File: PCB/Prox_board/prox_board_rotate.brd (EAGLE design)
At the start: 12 x 11 mm, 7 parts, among them U1 MAX44000

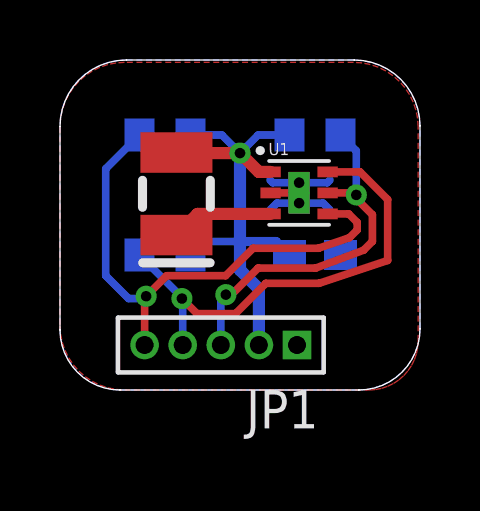
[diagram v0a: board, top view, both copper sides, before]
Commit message: Fix naming and silkscreen on the back of the board!
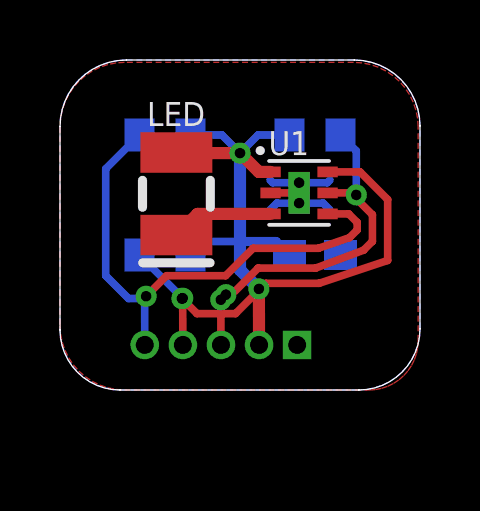
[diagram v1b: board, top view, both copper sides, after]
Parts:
- flipped JP1 to the bottom, turned to 0 degrees
- renumbered U$2 to LED
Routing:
- net SDA: track 15.8 -> 15.7 mm, vias 1 -> 2
- net VDD: vias 1 -> 2
- net SCL: vias 2 -> 3
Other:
- board text added: "LED"
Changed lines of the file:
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@@
 <layer number="23" name="tOrigins" color="15" fill="1" visible="yes" active="yes"/>
 <layer number="24" name="bOrigins" color="15" fill="1" visible="yes" active="yes"/>
-<layer number="25" name="tNames" color="7" fill="1" visible="no" active="yes"/>
-<layer number="26" name="bNames" color="7" fill="1" visible="no" active="yes"/>
+<layer number="25" name="tNames" color="7" fill="1" visible="yes" active="yes"/>
+<layer number="26" name="bNames" color="7" fill="1" visible="yes" active="yes"/>
 <layer number="27" name="tValues" color="7" fill="1" visible="no" active="yes"/>
 <layer number="28" name="bValues" color="7" fill="1" visible="no" active="yes"/>
@@
 <wire x1="12" y1="2.0366625" x2="12" y2="8.805565625" width="0" layer="20"/>
 <wire x1="12" y1="8.805565625" x2="9.805565625" y2="11" width="0" layer="20" curve="90"/>
+<text x="2.9" y="8.8" size="0.8" layer="25" ratio="14">LED</text>
 </plain>
 <attributes>
@@
 </autorouter>
 <elements>
-<element name="C1" library="resistor" package="C0603" value="0.1uF" x="8.5" y="4.5" rot="MR180"/>
-<element name="JP1" library="Wisp5_Harvester_Motor-driver_V2" package="PINHEAD_1X05-1.27MM" value="PINHEAD_PINHD-1X5-1.27MM" x="5.36" y="1.5" rot="R180"/>
-<element name="R1" library="resistor" package="R0603" value="DNP" x="3.5" y="8.5" rot="MR180"/>
-<element name="R2" library="resistor" package="R0603" value="DNP" x="3.5" y="4.5" rot="MR180"/>
-<element name="R3" library="resistor" package="R0603" value="DNP" x="8.5" y="8.5" rot="MR0"/>
-<element name="U$2" library="Wisp5_Harvester_Motor-driver_V2" package="MIDLED" value="SFH4651" x="3.88" y="6.54"/>
-<element name="U1" library="Wisp5_Harvester_Motor-driver_V2" package="6OTDFN-EP" value="MAX44000" x="6.97" y="5.57"/>
+<element name="C1" library="resistor" package="C0603" value="0.1uF" x="8.5" y="4.5" smashed="yes" rot="MR180">
+<attribute name="NAME" x="7.865" y="3.765" size="0.8" layer="26" rot="MR180"/>
+<attribute name="VALUE" x="7.865" y="6.405" size="0.8" layer="28" rot="MR180"/>
+</element>
+<element name="JP1" library="Wisp5_Harvester_Motor-driver_V2" package="PINHEAD_1X05-1.27MM" value="PINHEAD_PINHD-1X5-1.27MM" x="5.3654" y="1.5032" smashed="yes" rot="MR0">
+<attribute name="VALUE" x="8.5404" y="-1.3543" size="0.8" layer="28" rot="MR0"/>
+</element>
+<element name="R1" library="resistor" package="R0603" value="DNP" x="3.5" y="8.5" smashed="yes" rot="MR180">
+<attribute name="NAME" x="2.865" y="9.965" size="0.8" layer="26" rot="MR180"/>
+<attribute name="VALUE" x="2.865" y="10.405" size="0.8" layer="28" rot="MR180"/>
+</element>
+<element name="R2" library="resistor" package="R0603" value="DNP" x="3.5" y="4.5" smashed="yes" rot="MR180">
+<attribute name="NAME" x="2.765" y="3.765" size="0.8" layer="26" rot="MR180"/>
+<attribute name="VALUE" x="2.865" y="6.405" size="0.8" layer="28" rot="MR180"/>
+</element>
+<element name="R3" library="resistor" package="R0603" value="DNP" x="8.5" y="8.5" smashed="yes" rot="MR0">
+<attribute name="NAME" x="9.135" y="9.135" size="0.8" layer="26" rot="MR0"/>
+<attribute name="VALUE" x="9.135" y="6.595" size="0.8" layer="28" rot="MR0"/>
+</element>
+<element name="LED" library="Wisp5_Harvester_Motor-driver_V2" package="MIDLED" value="SFH4651" x="3.88" y="6.54" smashed="yes"/>
+<element name="U1" library="Wisp5_Harvester_Motor-driver_V2" package="6OTDFN-EP" value="MAX44000" x="6.97" y="5.57" smashed="yes">
+<attribute name="NAME" x="6.95" y="7.83" size="0.8" layer="25"/>
+</element>
 </elements>
 <signals>
@@
 </signal>
 <signal name="N$1">
-<contactref element="U$2" pad="C"/>
+<contactref element="LED" pad="C"/>
 <contactref element="U1" pad="3"/>
 <wire x1="7.02" y1="5.87" x2="4.585" y2="5.87" width="0.4064" layer="1"/>
@@
 <contactref element="JP1" pad="4"/>
 <contactref element="R2" pad="1"/>
-<wire x1="3.998371875" y1="3.151628125" x2="2.65" y2="4.5" width="0.254" layer="16"/>
-<wire x1="3.998371875" y1="3.151628125" x2="4.09" y2="3.06" width="0.254" layer="16"/>
-<wire x1="4.09" y1="3.06" x2="4.09" y2="1.5" width="0.254" layer="16"/>
+<wire x1="4.064" y1="3.086" x2="2.65" y2="4.5" width="0.254" layer="16"/>
+<wire x1="4.064" y1="3.086" x2="4.09" y2="3.06" width="0.254" layer="16"/>
+<wire x1="4.09" y1="3.06" x2="4.0954" y2="1.5032" width="0.254" layer="1"/>
 <wire x1="8.92" y1="7.27" x2="10.002" y2="7.27" width="0.254" layer="1"/>
 <wire x1="10.002" y1="7.27" x2="10.922" y2="6.35" width="0.254" layer="1"/>
@@
 <via x="4.064" y="3.048" extent="1-16" drill="0.35"/>
 <wire x1="4.064" y1="3.048" x2="4.064" y2="3.086" width="0.254" layer="16"/>
-<wire x1="4.064" y1="3.086" x2="3.998371875" y2="3.151628125" width="0.254" layer="16"/>
+<via x="4.09" y="3.06" extent="1-16" drill="0.35"/>
 </signal>
 <signal name="SCL">
@@
 <wire x1="8.52435" y1="4.064" x2="6.604" y2="4.064" width="0.254" layer="1"/>
 <wire x1="6.604" y1="4.064" x2="5.588" y2="3.048" width="0.254" layer="1"/>
-<wire x1="5.36" y1="3.00866875" x2="5.36" y2="1.5" width="0.254" layer="16"/>
+<wire x1="5.36" y1="3.00866875" x2="5.3654" y2="1.5032" width="0.254" layer="1"/>
 <wire x1="5.588" y1="3.048" x2="5.588" y2="3.11893125" width="0.254" layer="1"/>
 <wire x1="5.588" y1="3.11893125" x2="5.52913125" y2="3.1778" width="0.254" layer="1"/>
 <via x="5.52913125" y="3.1778" extent="1-16" drill="0.35"/>
 <wire x1="5.52913125" y1="3.1778" x2="5.36" y2="3.00866875" width="0.254" layer="16"/>
+<via x="5.36" y="3.00866875" extent="1-16" drill="0.35"/>
 </signal>
 <signal name="INT">
@@
 <wire x1="3.556" y1="3.81" x2="2.87098125" y2="3.12498125" width="0.254" layer="1"/>
 <wire x1="2.87098125" y1="3.12498125" x2="2.82" y2="3.074" width="0.254" layer="1"/>
-<wire x1="2.82" y1="3.074" x2="2.82" y2="1.5" width="0.254" layer="1"/>
+<wire x1="2.82" y1="3.074" x2="2.8254" y2="1.5032" width="0.254" layer="16"/>
 <wire x1="8.92" y1="5.87" x2="9.624" y2="5.87" width="0.254" layer="1"/>
 <wire x1="9.624" y1="5.87" x2="9.906" y2="5.588" width="0.254" layer="1"/>
@@
 <contactref element="U1" pad="1"/>
 <contactref element="C1" pad="1"/>
-<contactref element="U$2" pad="A"/>
+<contactref element="LED" pad="A"/>
 <wire x1="6" y1="4.949525" x2="6" y2="7.89699375" width="0.4064" layer="16"/>
 <wire x1="6" y1="4.949525" x2="6" y2="4" width="0.4064" layer="16"/>
@@
 <wire x1="6.62699375" y1="7.27" x2="7.02" y2="7.27" width="0.4064" layer="1"/>
 <wire x1="6" y1="4" x2="6.63" y2="3.37" width="0.4064" layer="16"/>
-<wire x1="6.63" y1="3.37" x2="6.63" y2="1.5" width="0.4064" layer="16"/>
+<wire x1="6.63" y1="3.37" x2="6.6354" y2="1.5032" width="0.4064" layer="1"/>
 <wire x1="7.65" y1="4.5" x2="7.200475" y2="4.949525" width="0.3048" layer="16"/>
 <wire x1="7.200475" y1="4.949525" x2="6" y2="4.949525" width="0.3048" layer="16"/>
@@
 <wire x1="4.35" y1="4.5" x2="4.799525" y2="4.949525" width="0.254" layer="16"/>
 <wire x1="4.799525" y1="4.949525" x2="6" y2="4.949525" width="0.254" layer="16"/>
+<via x="6.63" y="3.37" extent="1-16" drill="0.35"/>
 </signal>
 </signals>

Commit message: Final design for proximity and harvester board
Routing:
- net SCL: track 12.3 -> 12.8 mm, vias 3 -> 2
- net SDA: track 15.7 -> 15.9 mm, vias 2 -> 1
- net VDD: vias 2 -> 1
